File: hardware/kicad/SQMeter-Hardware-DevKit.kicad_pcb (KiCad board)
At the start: 2 copper layers, 125 x 82 mm, 46 parts, among them J1 12V IN, J10 AUX, J11 DevKitC-1 J1, J12 DevKitC-1 J3, J3 I2C TSL2591, J4 I2C MLX90614, J5 I2C BME280, J6 I2C SPARE, J7 GPS, J8 RG-15, J9 WIND, Q1 AO3401A, U1 AP63205WU, U4 USBLC6-2SC6, U5 USBLC6-2SC6, U6 USBLC6-2SC6

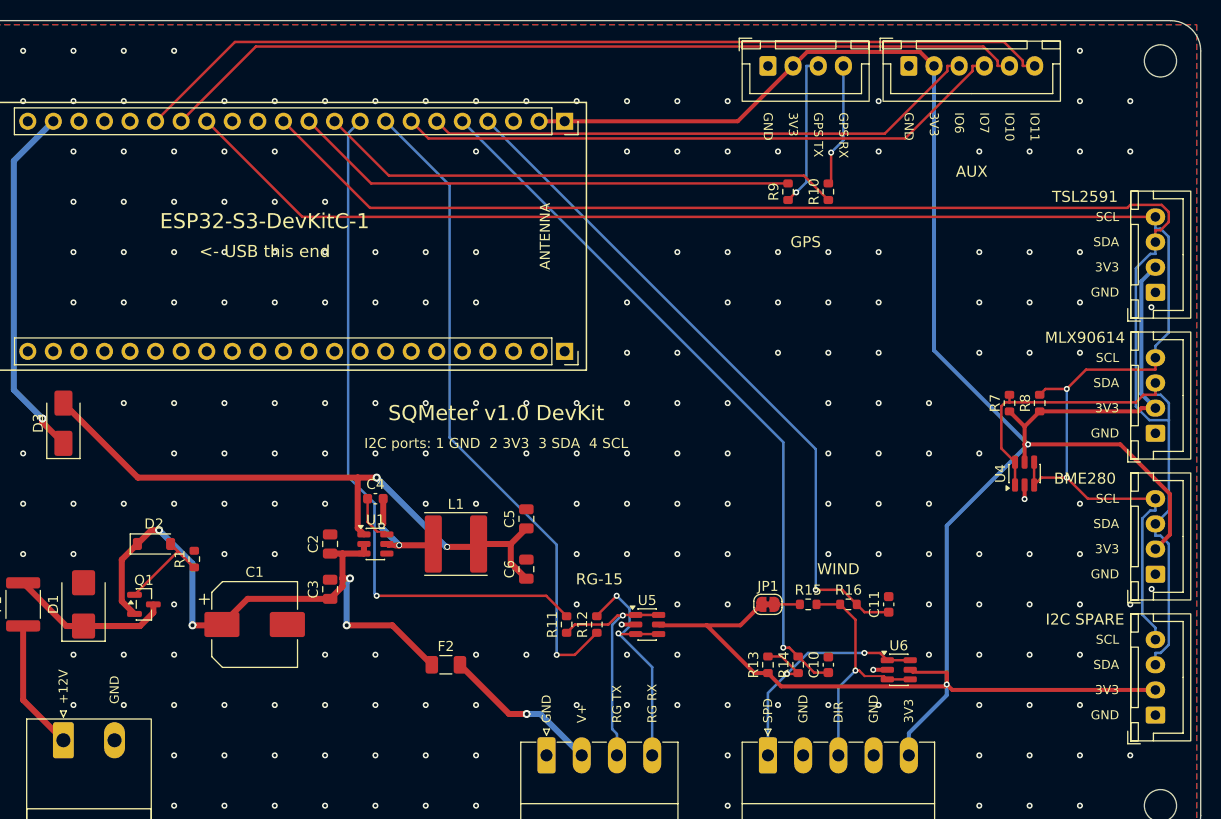
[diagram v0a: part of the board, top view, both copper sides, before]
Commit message: feat: Waveshare ESP32-S3-Zero socket variant and one GPIO map for all boards
- SQM_VARIANT=zero: ESP32-S3-Zero-M on 2x9 sockets (Waveshare pinout and
  drawing), same 5 V feed scheme as the DevKit variant
- GPIO map unified across module, DevKit and Zero (limited by the Zero's
  GPIO1-13 headers): RG-15 1/2, wind 4/5, I2C 8/9, GPS 12/13, AUX 6/7/10/11
- fab exports for all three
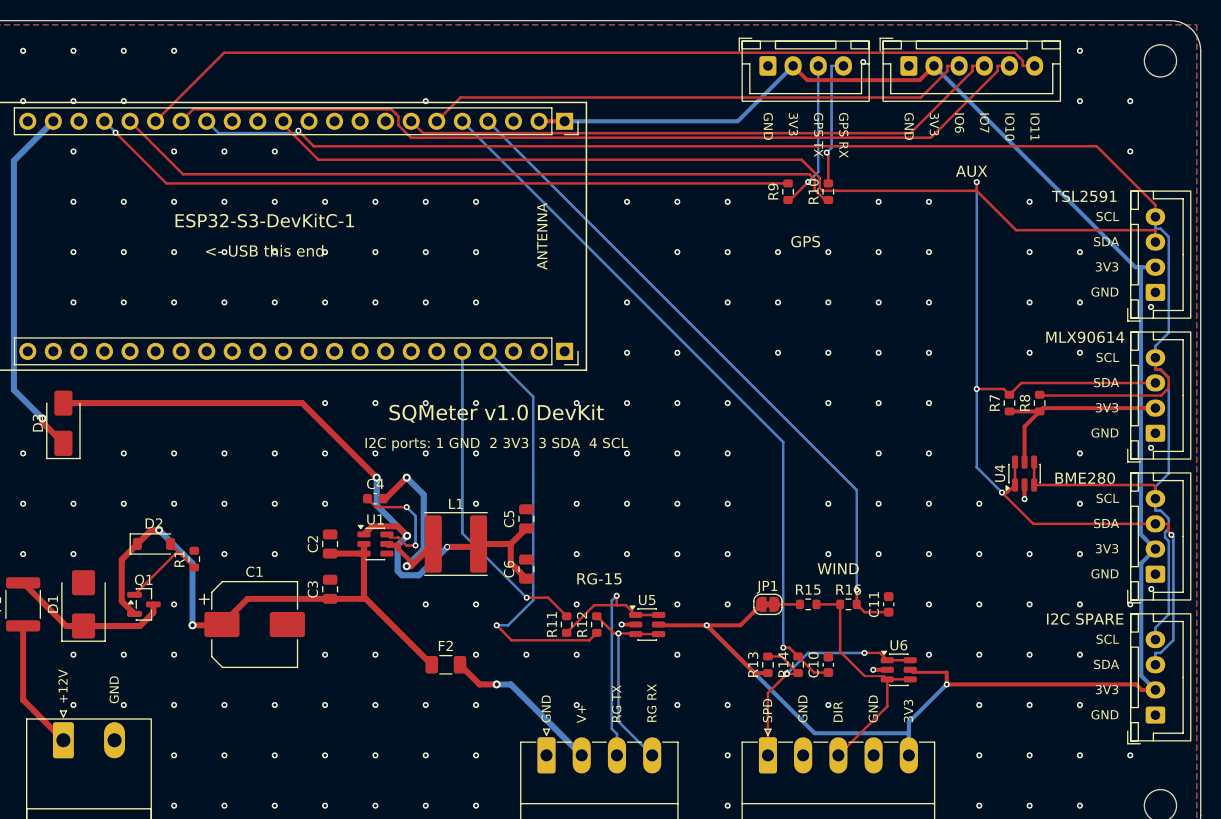
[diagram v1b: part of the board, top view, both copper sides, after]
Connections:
- J11 pad 10: /GPS_TX -> (no net)
- J11 pad 11: /GPS_RX -> (no net)
- J11 pad 18: (no net) -> /GPS_TX
- J11 pad 19: (no net) -> /GPS_RX
- J11 pad 8: /RG_TX -> (no net)
- J11 pad 9: /RG_RX -> (no net)
- J12 pad 4: (no net) -> /RG_TX
- J12 pad 5: (no net) -> /RG_RX
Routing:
- net /RG_RX: track 68.5 -> 31.9 mm
- net +3V3: track 240.5 -> 216.6 mm
- net /RG_TX: track 65.0 -> 42.1 mm
- net /GPS_TX: track 52.3 -> 73.2 mm
- net /GPS_RX: track 50.2 -> 70.5 mm, vias 0 -> 1
- net /SCL: track 167.0 -> 178.2 mm, vias 2 -> 1
- net /SW: track 10.2 -> 20.9 mm
- net /SDA: track 174.3 -> 181.3 mm, vias 0 -> 4
- net /BST: track 4.74 -> 11.7 mm, vias 0 -> 2
- net +5V: track 62.7 -> 69.1 mm, vias 2 -> 3
- net /RG_RXI: track 25.2 -> 20.4 mm, vias 2 -> 1
- net /RG_TXO: track 24.5 -> 27.9 mm
- net +12V: track 61.4 -> 58.1 mm, vias 4 -> 2
- net /WIND_DIR: track 68.2 -> 66.7 mm
- net /AUX3: track 86.5 -> 87.7 mm
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
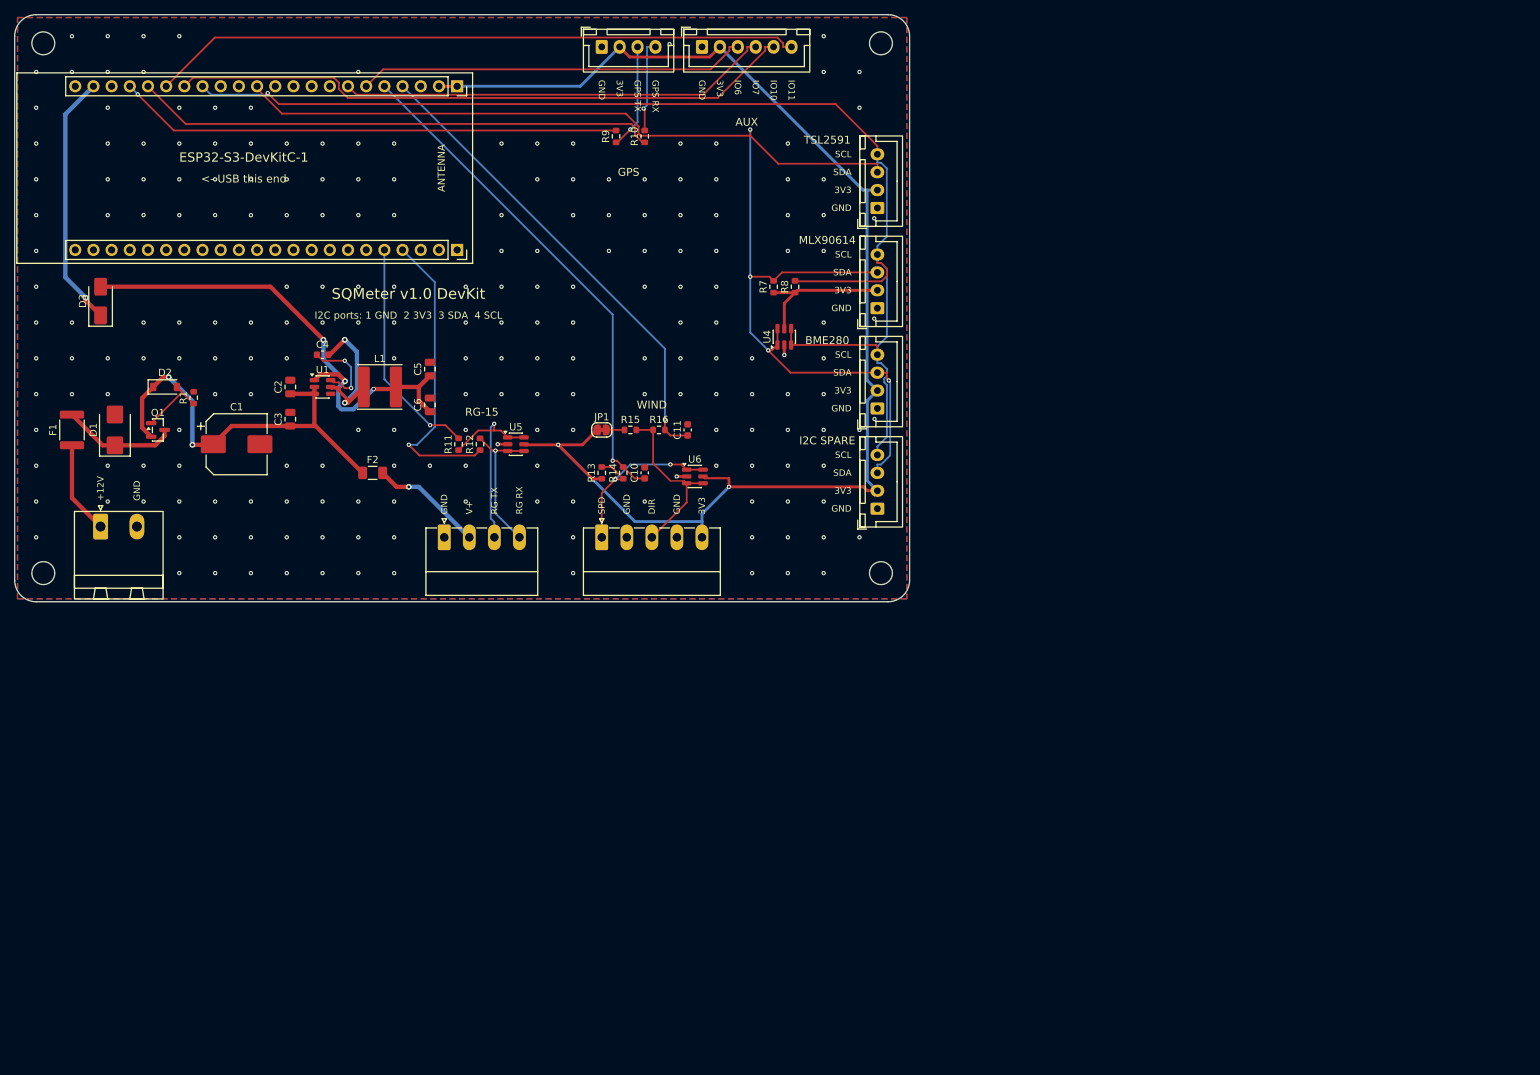
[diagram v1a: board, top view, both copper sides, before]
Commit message: fix: centre boards on the A4 sheet instead of hanging off the page origin
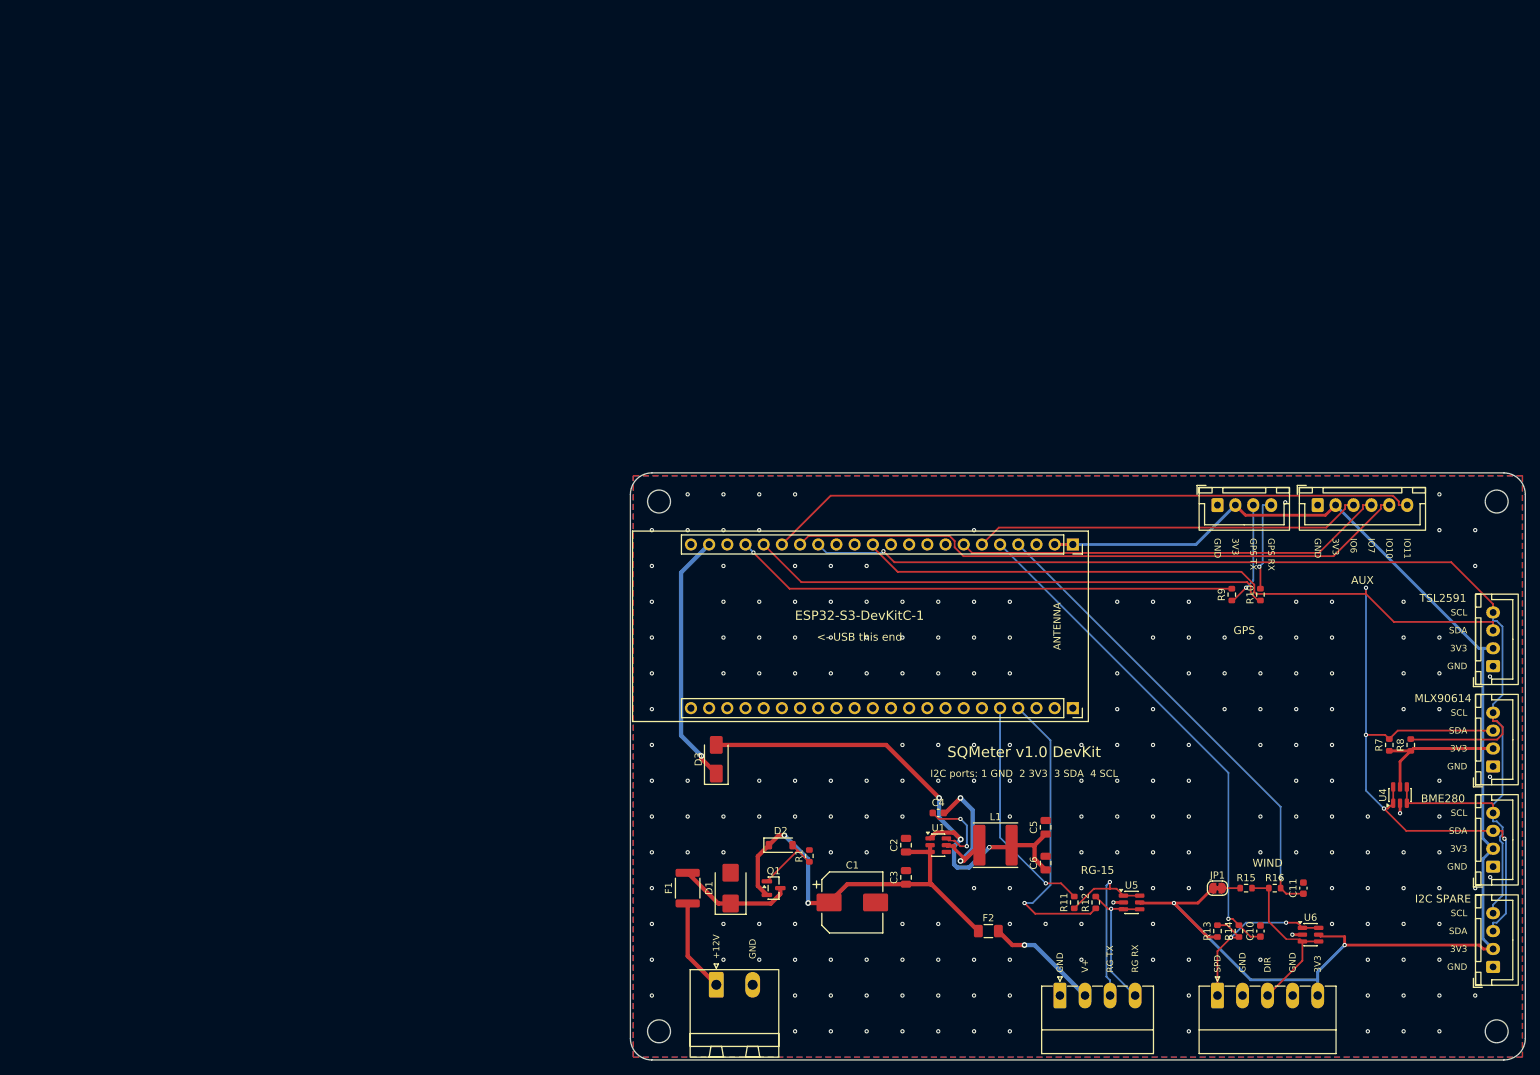
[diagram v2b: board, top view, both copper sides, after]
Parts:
- moved J11 107.2 mm to (147.8, 74.0)
- moved J12 107.2 mm to (147.8, 96.9)
- moved C1 107.2 mm to (117.0, 124.0)
- moved C10 107.2 mm to (174.0, 128.0)
- moved C11 107.2 mm to (180.0, 122.0)
- moved C2 107.2 mm to (124.5, 116.0)
- moved C3 107.2 mm to (124.5, 120.5)
- moved C4 107.2 mm to (129.0, 111.5)
- moved C5 107.2 mm to (144.0, 113.5)
- moved C6 107.2 mm to (144.0, 118.5)
- moved D1 107.2 mm to (100.0, 122.0)
- moved D2 107.2 mm to (107.0, 116.0)
- moved D3 107.2 mm to (98.0, 104.0)
- moved F1 107.2 mm to (94.0, 122.0)
- moved F2 107.2 mm to (136.0, 128.0)
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
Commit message: feat: second I2C bus for a second TSL2591 (SQM + SQM-L)
TSL2591 has a fixed address, so the second sensor gets its own bus on
GPIO10/11 (I2C-2 JST-XH port, own pull-ups and ESD). AUX drops to IO6/IO7.
Q1 gate zener replaced by a resistor divider (one fewer extended part).
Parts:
- removed D2: BZT52C10, Diode_SMD:D_SOD-123
- added J13: I2C-2 TSL2591 #2, Connector_JST:JST_XH_B4B-XH-A_1x04_P2.50mm_Vertical, F.Cu at (195.0, 68.5)
- added R19: 10k, Resistor_SMD:R_0603_1608Metric, F.Cu at (107.0, 115.0)
- added R20: 4.7k, Resistor_SMD:R_0603_1608Metric, F.Cu at (185.0, 82.5)
- added R21: 4.7k, Resistor_SMD:R_0603_1608Metric, F.Cu at (188.0, 82.5)
- added U7: USBLC6-2SC6, Package_TO_SOT_SMD:SOT-23-6, F.Cu at (192.0, 85.0)
- J10: footprint Connector_JST:JST_XH_B6B-XH-A_1x06_P2.50mm_Vertical -> Connector_JST:JST_XH_B4B-XH-A_1x04_P2.50mm_Vertical
- J3: value I2C TSL2591 -> I2C TSL2591 #1
- moved H2 7.52 mm to (207.5, 75.5)
- moved J10 0.50 mm to (181.5, 68.5)
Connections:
- J11 pad 16: /AUX3 -> /SDA2
- J11 pad 17: /AUX4 -> /SCL2
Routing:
- net /SCL2: track 0.00 -> 125.6 mm
- net /SDA2: track 0.00 -> 111.4 mm, vias 0 -> 1
- net /AUX4: track 91.0 -> 0.00 mm
- net /AUX3: track 87.7 -> 0.00 mm
- net +3V3: track 216.6 -> 238.2 mm
- net /Q1_G: track 9.42 -> 19.6 mm, vias 0 -> 2
- net /SCL: track 178.2 -> 168.5 mm
- net /RG_RXI: track 20.4 -> 25.1 mm, vias 1 -> 2
- net /WSPD_EXT: track 27.1 -> 31.4 mm
- net /RG_TXO: track 27.9 -> 23.6 mm
- net /RG_TX: track 42.1 -> 37.9 mm
- net /RG_RX: track 31.9 -> 35.2 mm
- net /GPS_RX: track 70.5 -> 73.5 mm, vias 1 -> 0
- net /SDA: track 181.3 -> 178.5 mm, vias 4 -> 2
- net +12V: track 58.1 -> 55.5 mm, vias 2 -> 0
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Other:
- board text added: "I2C-2"
- board text added: "TSL2591 #1"
- board text removed: "IO10"
- board text removed: "IO11"
- board text removed: "TSL2591"

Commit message: feat: brand lockup on silkscreen, hardware Rev A, JLC-ready gerber zips
- SQMeter lockup (brand kit silkscreen mark + Inter SemiBold name) as plain
  silkscreen polygons from brand_silk.json; no font install needed
- HW_REV = A: on the silkscreen, KiCad title blocks, gerber metadata and fab
  file names; versioned separately from firmware
- drop the verbose I2C pinout line; per-pin labels already cover it
- gerber zip holds only fab layers + drill files
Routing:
- net +3V3: track 238.2 -> 262.3 mm, vias 2 -> 5
- net /SDA: track 178.5 -> 156.4 mm, vias 2 -> 1
- net /SCL: track 168.5 -> 183.6 mm
- net +5V: track 69.2 -> 57.6 mm, vias 3 -> 2
- net /RG_TXO: track 23.6 -> 29.2 mm, vias 1 -> 2
- net /GPS_TXO: track 14.6 -> 19.1 mm, vias 0 -> 1
- net /RG_RXI: track 25.1 -> 21.1 mm, vias 2 -> 1
- net /WDIR_EXT: track 24.5 -> 28.4 mm, vias 1 -> 2
- net /VIN_F: track 16.1 -> 19.9 mm
- net /GPS_RX: track 73.5 -> 70.5 mm
- net /RG_TX: track 37.9 -> 36.1 mm
- net /BST: track 11.7 -> 10.0 mm, vias 2 -> 0
- net /AUX2: track 61.6 -> 63.0 mm, vias 0 -> 1
- net /SDA2: track 111.4 -> 110.4 mm, vias 1 -> 0
- net /RG_PWR: track 16.6 -> 15.8 mm
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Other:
- board text added: "Rev A DevKitC-1"
- board text removed: "I2C ports: 1 GND 2 3V3 3 SDA 4 SCL"
- board text removed: "SQMeter v1.0 DevKit"

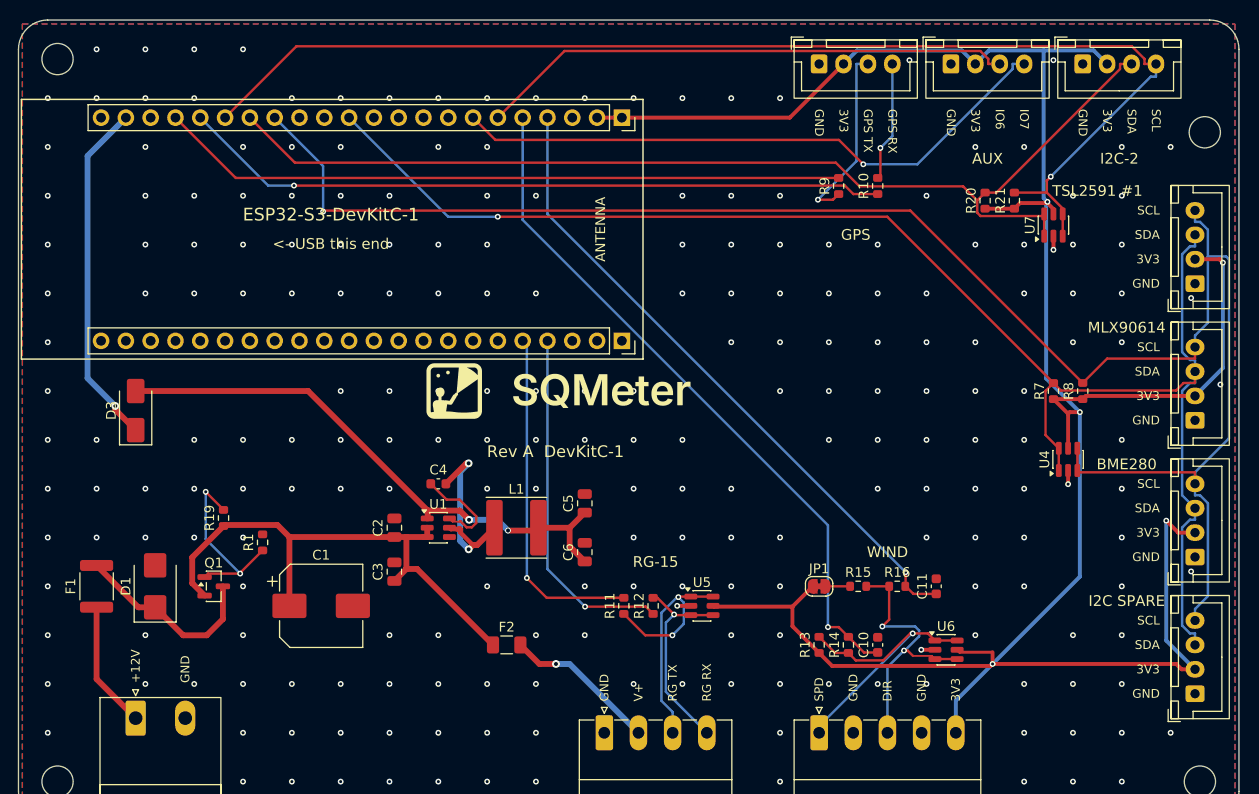
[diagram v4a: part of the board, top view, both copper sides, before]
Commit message: feat: Inter Bold silkscreen (embedded), black mask / white silk stackup
- all silkscreen text and references in Inter Bold, min 1.2 mm; font embedded in
  the board files so they open the same without Inter installed
- stroke widths measured on plotted gerbers (>0.15 mm); KiCad's TrueType
  thickness check ignored as it flags every size of the variable font
- stackup: black solder mask, white silkscreen (3D view; colour is picked at order)
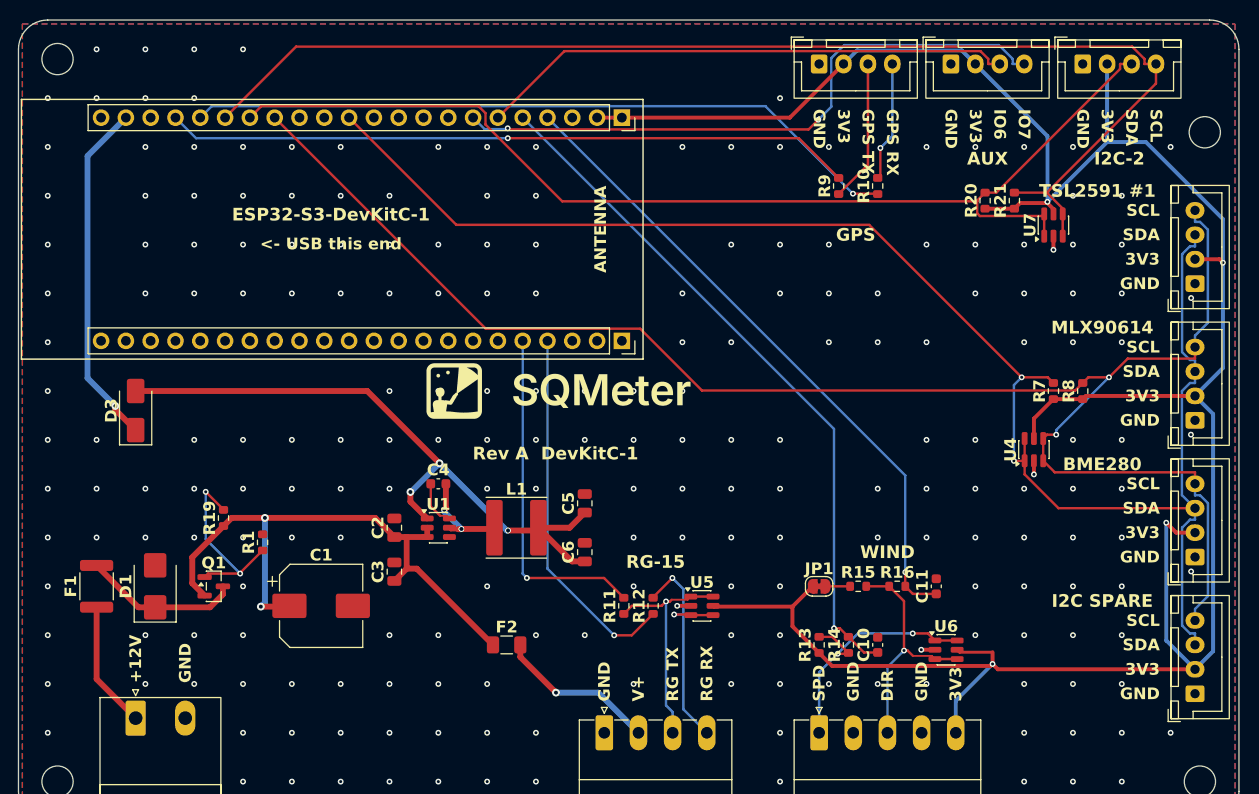
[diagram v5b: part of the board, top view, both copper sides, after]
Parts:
- moved U4 3.64 mm to (190.0, 108.0)
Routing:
- net /SCL: track 183.6 -> 168.3 mm, vias 1 -> 2
- net /SW: track 19.6 -> 10.2 mm
- net +5V: track 57.6 -> 66.5 mm, vias 2 -> 3
- net /SDA: track 156.4 -> 162.8 mm, vias 1 -> 2
- net +12V: track 55.5 -> 61.3 mm, vias 0 -> 2
- net /RG_TXO: track 29.2 -> 23.6 mm, vias 2 -> 1
- net /BST: track 10.0 -> 4.74 mm
- net /GPS_TXO: track 19.1 -> 14.6 mm, vias 1 -> 0
- net /RG_RXI: track 21.1 -> 25.1 mm, vias 1 -> 2
- net /WDIR_EXT: track 28.4 -> 24.5 mm, vias 2 -> 1
- net /VIN_F: track 19.9 -> 16.1 mm
- net /WSPD_EXT: track 30.8 -> 27.1 mm, vias 1 -> 2
- net +3V3: track 262.3 -> 260.1 mm, vias 5 -> 4
- net /RG_TX: track 36.1 -> 37.9 mm
- net /SDA2: track 110.4 -> 112.2 mm
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
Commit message: feat: ESP32-S3-ETH PoE home board and Li-ion travel board
- eth: Waveshare ESP32-S3-ETH (+ PoE module) on 2x20 sockets, PoE or 12 V in,
  MT3608 boost keeps the RG-15 at 12.6 V on PoE; own GPIO map (W5500 owns 9-14)
- travel: ESP32-S3-Zero, USB-C only, MCP73871 power-path Li-ion charger with
  NTC cold-charge cut-off, power slide switch, battery/charger status on GPIO,
  OLED port; 85 x 66 mm, no field wiring
- connector titles placed relative to their connector so layouts can differ
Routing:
- net /SW: track 10.2 -> 20.9 mm
- net +3V3: track 260.1 -> 250.1 mm, vias 4 -> 5
- net /BST: track 4.74 -> 11.9 mm, vias 0 -> 2
- net +5V: track 66.5 -> 70.8 mm
- net /AUX2: track 64.6 -> 60.5 mm, vias 2 -> 0
- net /SDA: track 162.8 -> 166.0 mm, vias 2 -> 3
- net /GPS_RX: track 70.5 -> 73.6 mm, vias 1 -> 0
- net /SCL: track 168.3 -> 170.6 mm
- net +12V: track 61.3 -> 59.0 mm
- net /SDA2: track 112.2 -> 110.5 mm, vias 0 -> 1
- net /GPS_TX: track 73.6 -> 74.8 mm, vias 1 -> 3
- net /WIND_DIR: track 66.7 -> 67.8 mm
- net GND: vias 220 -> 217
